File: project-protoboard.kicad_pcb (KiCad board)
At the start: 2 copper layers, 50.8 x 81.3 mm, 80 parts, among them J1 SM04B-SRSS-TB(LF)(SN), J10 Conn_01x06_Socket, J11 Conn_01x06_Socket, J12 Conn_01x06_Socket, J13 Conn_01x06_Socket, J14 Conn_01x06_Socket, J15 Conn_01x06_Socket, J16 Conn_01x06_Socket, J17 Conn_01x06_Socket, J18 Conn_01x05_Socket, J19 Conn_01x05_Socket, J2 Conn_01x04_Socket, J20 Conn_01x05_Socket, J21 Conn_01x05_Socket, J22 Conn_01x06_Socket, J23 Conn_01x06_Socket, J24 Conn_01x06_Socket, J25 Conn_01x06_Socket, J26 Conn_01x06_Socket, J27 Conn_01x06_Socket, J28 Conn_01x06_Socket, J29 Conn_01x06_Socket, J3 Conn_01x09_Socket, J30 Conn_01x06_Socket, J31 Conn_01x06_Socket, J32 Conn_01x06_Socket, J33 Conn_01x06_Socket, J34 Conn_01x06_Socket, J35 Conn_01x06_Socket, J36 Conn_01x06_Socket, J37 Conn_01x30_Socket, J38 Conn_01x30_Socket, J39 Conn_01x06_Socket, J4 Conn_01x13_Socket, J40 Conn_01x06_Socket, J41 Conn_01x06_Socket, J42 Conn_01x06_Socket, J43 Conn_01x06_Socket, J44 Conn_01x06_Socket, J45 Conn_01x06_Socket, J46 Conn_01x06_Socket, J47 Conn_01x06_Socket, J48 Conn_01x06_Socket, J49 Conn_01x06_Socket, J5 Conn_01x09_Socket, J50 Conn_01x06_Socket, J51 Conn_01x06_Socket, J52 Conn_01x06_Socket, J53 Conn_01x06_Socket, J54 Conn_01x06_Socket, J55 Conn_01x06_Socket, J56 Conn_01x06_Socket, J57 Conn_01x06_Socket, J58 Conn_01x06_Socket, J59 Conn_01x06_Socket, J6 Conn_01x13_Socket, J60 Conn_01x06_Socket, J61 Conn_01x06_Socket, J62 Conn_01x06_Socket, J63 Conn_01x06_Socket, J64 Conn_01x06_Socket, J65 Conn_01x06_Socket, J66 Conn_01x06_Socket, J67 Conn_01x06_Socket, J68 Conn_01x06_Socket, J69 Conn_01x26_Socket, J7 Conn_01x06_Socket, J70 Conn_01x26_Socket, J8 Conn_01x06_Socket, J9 Conn_01x06_Socket

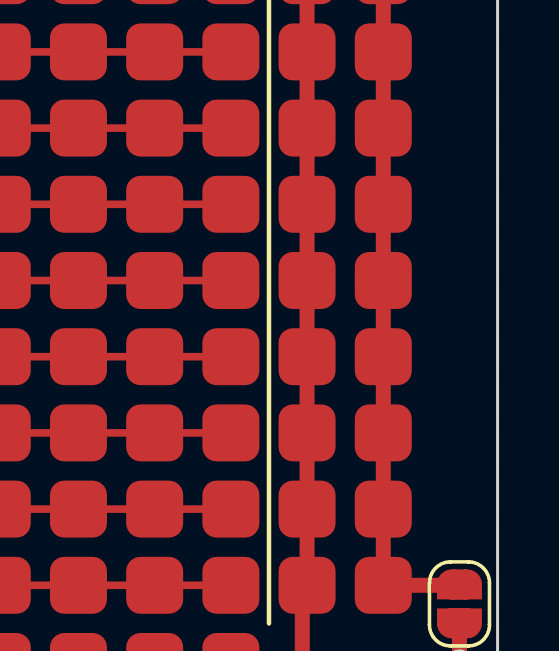
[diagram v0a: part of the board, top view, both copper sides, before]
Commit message: Add a version silkscreen
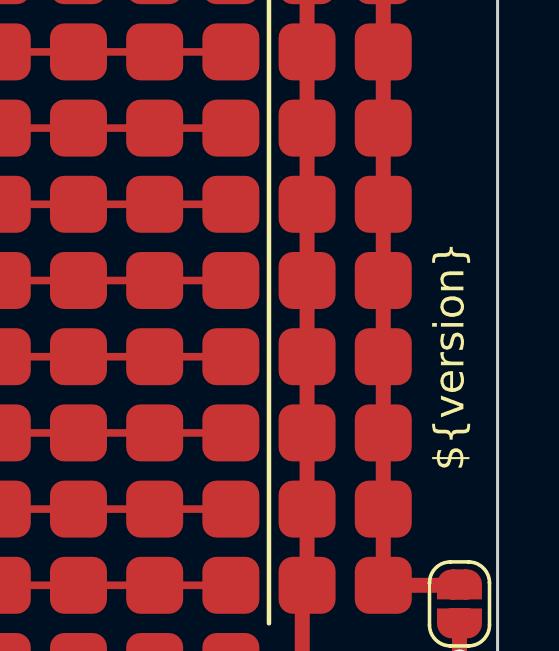
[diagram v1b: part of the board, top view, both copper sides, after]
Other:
- board text added: "${version}"
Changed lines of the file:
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@@
+    (effects (font (size 1 1) (thickness 0.15)) (justify left bottom))
+  )
+  (gr_text "${version}" (at 122.174 87.63 90) (layer "F.SilkS")
     (effects (font (size 1 1) (thickness 0.15)) (justify left bottom))
   )
